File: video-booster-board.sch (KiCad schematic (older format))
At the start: 133 parts, among them IC1 INA180A1IDBVT, J1 0473460001, J10 M20-9990246, J11 MC-HVT1-S04-G, J2 HDMI-PE10-19-LF, J3 HDMI-PE10-19-LF, J6 685119134923_, J9 685119134923_, SW1 1571983-5, U1 PTN3363, U2 TPS2110APW, U3 PTN3363, U4 LP2985-33DBVR, U5 NTS0102GT, U6 EFM32HG321, U7 NTS0102GT

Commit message: Added pulldown on PWR_CTL_D1 and  TVS protection on USB
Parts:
- removed D10: RCLAMP0524PATCT, video-booster-board-footprints:UFDFN-10_2.5x1mm, symbol video-booster-board:RCLAMP0524PATCT
- added D10, D11: RCLAMP0524PATCT_, video-booster-board-footprints:UFDFN-10_2.5x1mm, symbol video-booster-board:RCLAMP0524PATCT_
- added R60: R_100k_0402, video-booster-board-footprints:0402-res, symbol video-booster-board:R_100k_0402-
- C1, C36: symbol video-booster-board:C_4u7_0603-antmicroCapacitors0603 -> video-booster-board:C_4u7_0603-
- C10, C11, C12, C13, C14, C15, C16, C18, C19, C2, C20, C21, C22, C23, C24, C25, C27, C3, C31, C32, C33, C35, C38, C39, C40, C7, C8, C9: symbol video-booster-board:C_100n_0402_6V3-antmicroCapacitors0402 -> video-booster-board:C_100n_0402_6V3-
- C17, C4: symbol video-booster-board:C_10u_0603-antmicroCapacitors0603 -> video-booster-board:C_10u_0603-
- C26, C34, C37, C5, C6: symbol video-booster-board:C_1u_0402-antmicroCapacitors0402 -> video-booster-board:C_1u_0402-
- C28, C30: symbol video-booster-board:C_2u2_0402-antmicroCapacitors0402 -> video-booster-board:C_2u2_0402-
- C29: symbol video-booster-board:C_10n_0402-antmicroCapacitors0402 -> video-booster-board:C_10n_0402-
- J1: symbol video-booster-board:0473460001-antmicroUSBDVIHDMIConnectors -> video-booster-board:0473460001-
- J11: symbol video-booster-board:MC-HVT1-S04-G-antmicroRectangularConnectorsHeadersMalePins -> video-booster-board:MC-HVT1-S04-G-
- J2, J3: symbol video-booster-board:HDMI-PE10-19-LF-antmicroUSBDVIHDMIConnectors -> video-booster-board:HDMI-PE10-19-LF-
- J6, J9: symbol video-booster-board:685119134923_-antmicroUSBDVIHDMIConnectors -> video-booster-board:685119134923_-
- R1, R2: symbol video-booster-board:R_15R_0402-antmicroResistors0402 -> video-booster-board:R_15R_0402-
- R10, R21, R22, R23, R26, R28, R29, R31, R32, R34, R35, R36, R37, R39, R40, R58, R59, R9: symbol video-booster-board:R_10k_0402-antmicroResistors0402 -> video-booster-board:R_10k_0402-
- R11, R12, R7, R8: symbol video-booster-board:R_0R_0402-antmicroResistors0402 -> video-booster-board:R_0R_0402-
- R13, R17: symbol video-booster-board:R_12k4_0402-antmicroResistors0402 -> video-booster-board:R_12k4_0402-
- R14, R15, R19, R24, R5, R6: symbol video-booster-board:R_100k_0402-antmicroResistors0402 -> video-booster-board:R_100k_0402-
- R3, R33, R42, R43, R44, R45, R46, R47, R48, R49, R50, R51, R52, R53, R54, R55: symbol video-booster-board:R_49R9_0402-antmicroResistors0402 -> video-booster-board:R_49R9_0402-
- U1, U3: symbol video-booster-board:PTN3363-antmicroInterfaceDriversReceiversTransceivers -> video-booster-board:PTN3363-
- U4: symbol video-booster-board:LP2985-33DBVR-antmicroPMICVoltageRegulatorsLinear -> video-booster-board:LP2985-33DBVR-
- U6: symbol video-booster-board:EFM32HG321-antmicroMicrocontrollers -> video-booster-board:EFM32HG321-
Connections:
- net labels added: UDN, UDP
- wire segments 560 -> 574

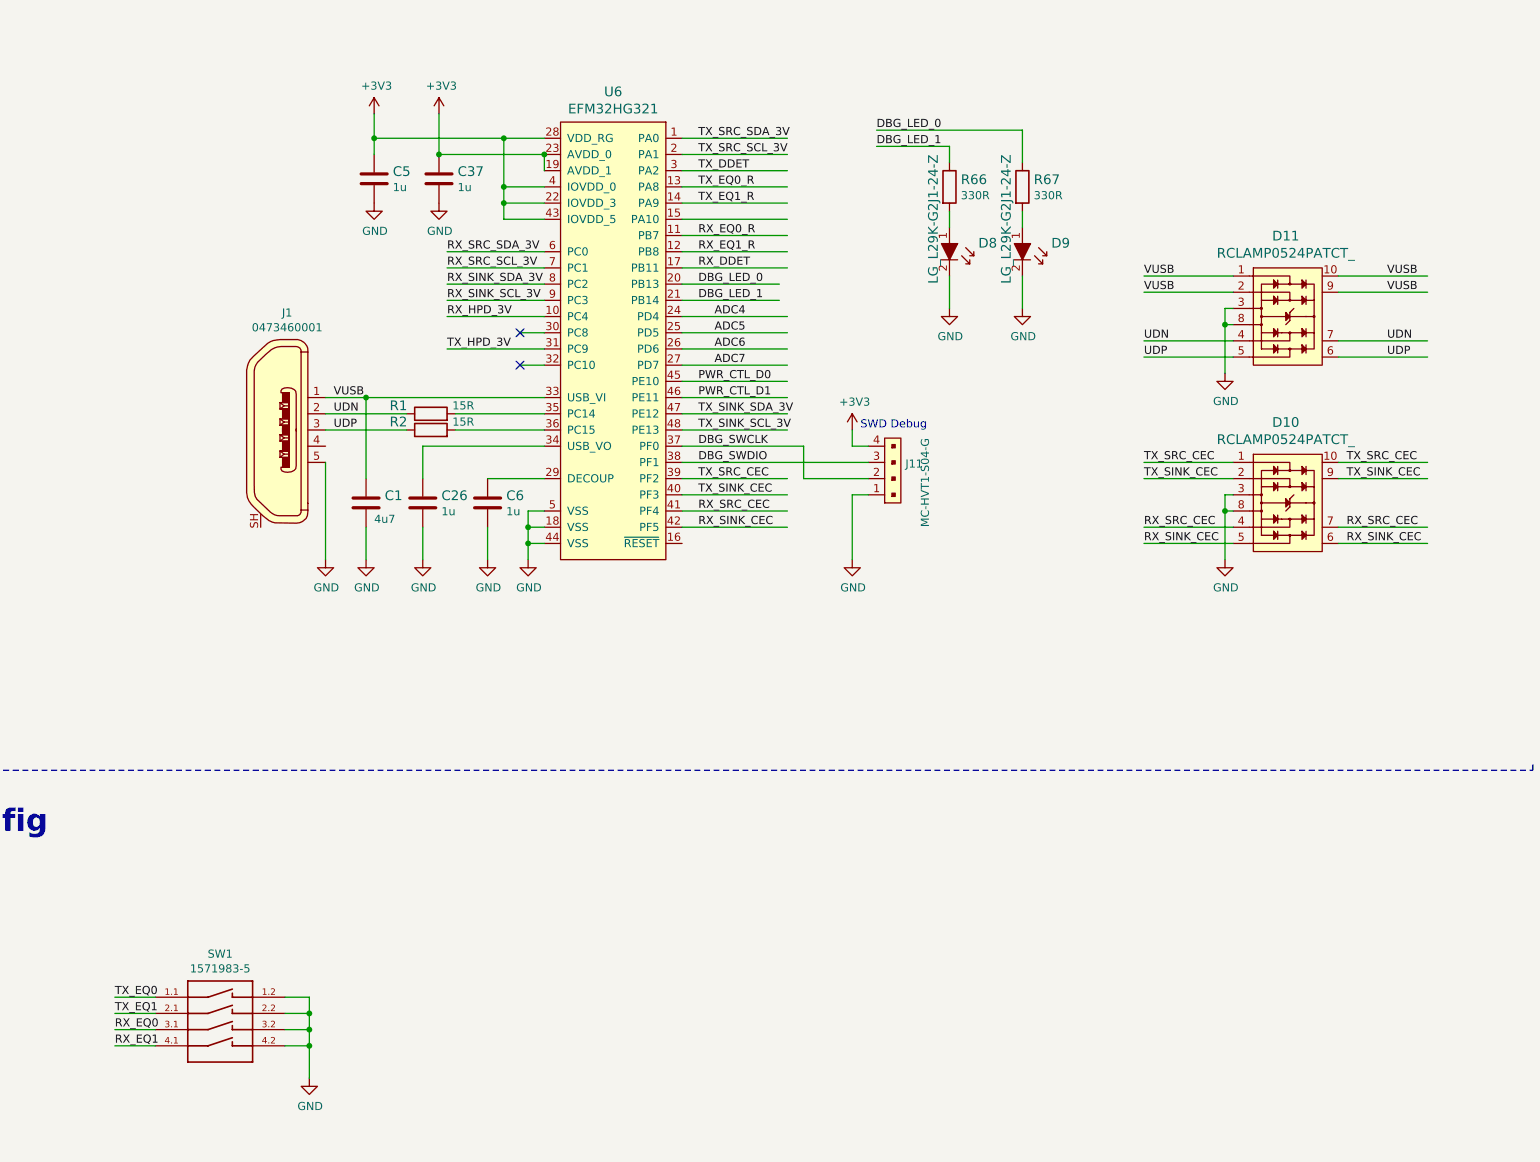
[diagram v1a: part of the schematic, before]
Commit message: PCB routing: HDMI,control, USB
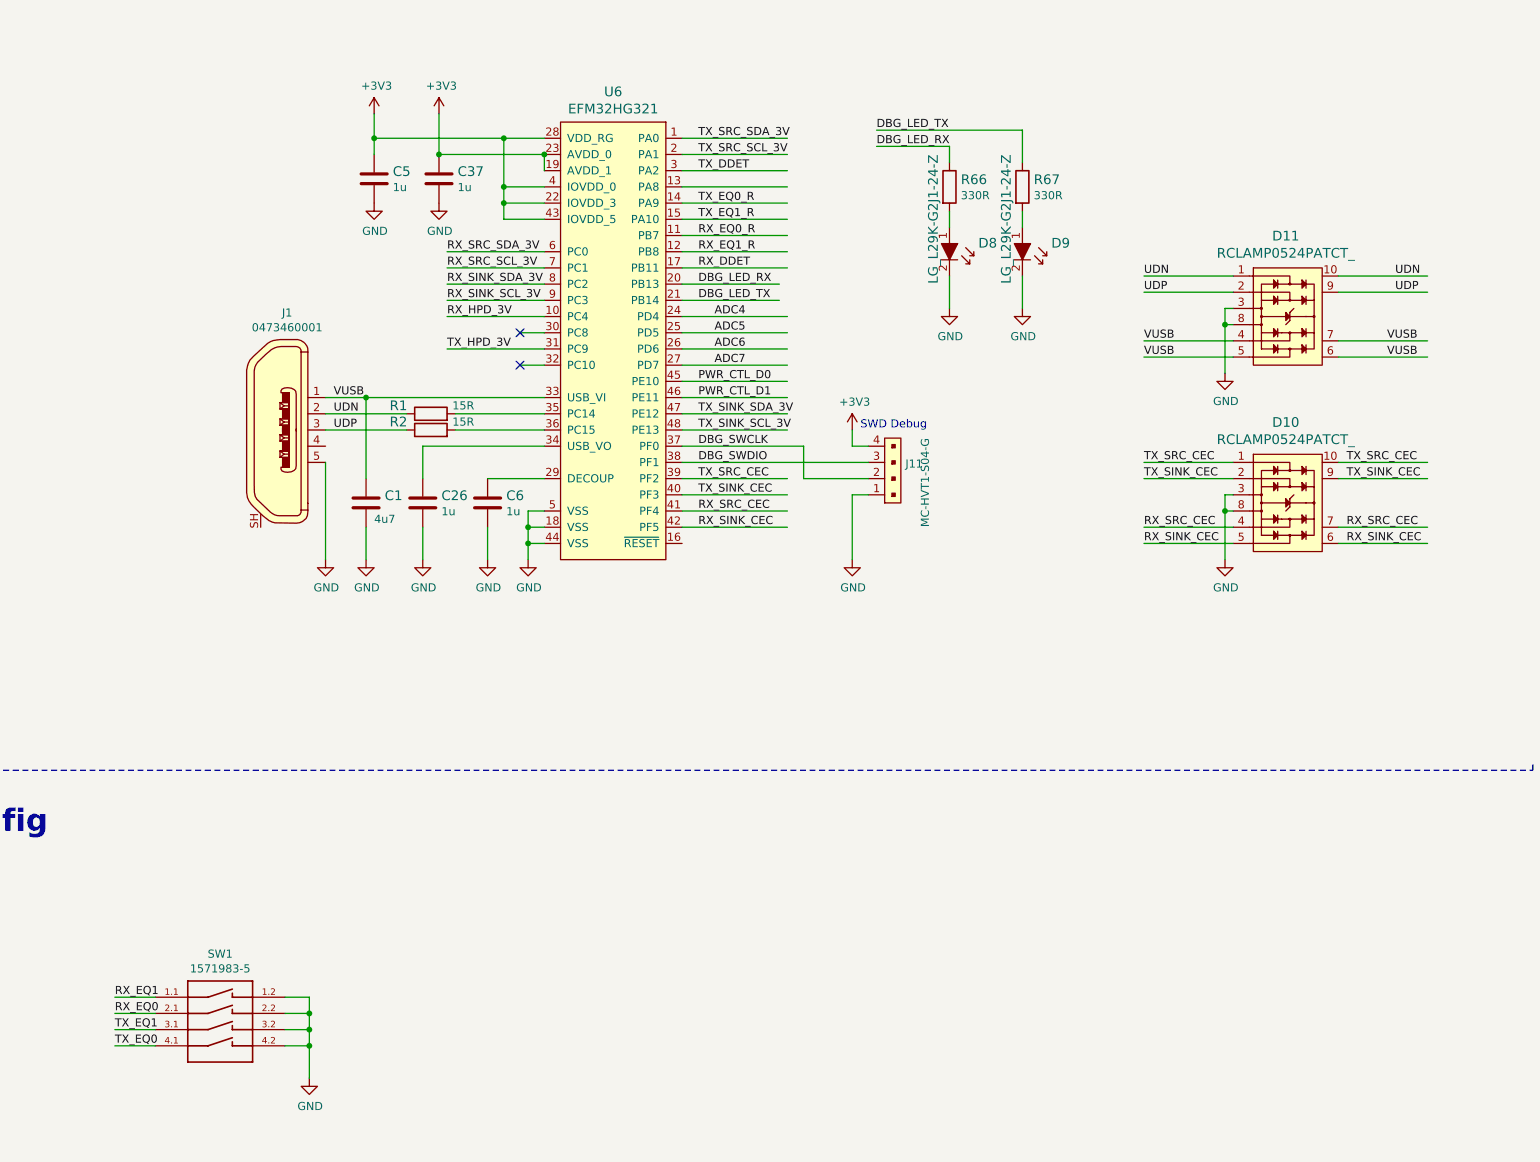
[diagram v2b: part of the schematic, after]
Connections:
- net labels added: DBG_LED_RX, DBG_LED_TX
- net labels removed: DBG_LED_0, DBG_LED_1
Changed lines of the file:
@@
 Wire Wire Line
 	5700 9600 5550 9600
-Text Label 17800 9400 0    50   ~ 0
+Text Label 17800 9500 0    50   ~ 0
 TX_EQ0_R
-Text Label 17800 9500 0    50   ~ 0
+Text Label 17800 9600 0    50   ~ 0
 TX_EQ1_R
 Text Label 17800 9700 0    50   ~ 0
@@
 Wire Wire Line
 	17700 10800 18350 10800
+Text Label 17800 10100 0    50   ~ 0
+DBG_LED_TX
 Text Label 17800 10000 0    50   ~ 0
-DBG_LED_0
-Text Label 17800 10100 0    50   ~ 0
-DBG_LED_1
+DBG_LED_RX
 Wire Wire Line
 	18750 11700 18750 11300
@@
 	16750 11500 16750 11600
 Text Label 18900 9150 0    50   ~ 0
-DBG_LED_1
+DBG_LED_RX
 Text Label 18900 9050 0    50   ~ 0
-DBG_LED_0
+DBG_LED_TX
 Wire Wire Line
 	19800 9050 19800 9250
@@
 Wire Wire Line
 	14200 14700 14450 14700
+Text Label 14200 14700 0    50   ~ 0
+TX_EQ0
+Text Label 14200 14600 0    50   ~ 0
+TX_EQ1
+Text Label 14200 14500 0    50   ~ 0
+RX_EQ0
 Text Label 14200 14400 0    50   ~ 0
-TX_EQ0
-Text Label 14200 14500 0    50   ~ 0
-TX_EQ1
-Text Label 14200 14600 0    50   ~ 0
-RX_EQ0
-Text Label 14200 14700 0    50   ~ 0
 RX_EQ1
 $Comp
@@
 Text Label 15550 10900 0    50   ~ 0
 UDP
+Text Label 20550 10350 0    50   ~ 0
+VUSB
 Text Label 20550 9950 0    50   ~ 0
-VUSB
-Text Label 20550 10350 0    50   ~ 0
 UDN
+Text Label 20550 10050 0    50   ~ 0
+UDP
 Text Label 20550 10450 0    50   ~ 0
-UDP
-Text Label 20550 10050 0    50   ~ 0
-VUSB
-Text Label 22050 9950 0    50   ~ 0
 VUSB
 Text Label 22050 10350 0    50   ~ 0
+VUSB
+Text Label 22100 9950 0    50   ~ 0
 UDN
+Text Label 22100 10050 0    50   ~ 0
+UDP
 Text Label 22050 10450 0    50   ~ 0
-UDP
-Text Label 22050 10050 0    50   ~ 0
 VUSB
 $Comp

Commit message: Routing completed. Minor changes in control pins placement
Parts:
- removed R11, R12, R7, R8: R_0R_0402, video-booster-board-footprints:0402-res, symbol video-booster-board:R_0R_0402-
- removed R22, R28: R_10k_0402, video-booster-board-footprints:0402-res, symbol video-booster-board:R_10k_0402-
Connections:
- wire segments 574 -> 564
- no-connect marks 2 -> 1
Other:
- note removed: "DNP"
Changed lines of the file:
@@
 	0    1    1    0
 $EndComp
-$Comp
-L video-booster-board:R_10k_0402- R22
-U 1 1 5DBDC2E5
-P 4800 5700
-F 0 "R22" V 4650 5750 60  0000 L CNN
-F 1 "R_10k_0402" H 4800 5550 60  0001 C CNN
-F 2 "video-booster-board-footprints:0402-res" H 5000 5900 60  0001 L CNN
-F 3 "" H 4800 5700 50  0001 C CNN
-F 4 "VISHAY" H 5000 6100 60  0001 L CNN "Manufacturer"
-F 5 "CRCW040210K0FKEDHP" H 5000 6000 60  0001 L CNN "MPN"
-F 6 "10k" V 4950 5750 50  0000 L CNN "Val"
-	1    4800 5700
-	0    1    1    0
-$EndComp
 Wire Wire Line
 	4900 6150 4800 6150
@@
 	1    0    0    -1
 $EndComp
-Text Notes 4850 5700 0    50   ~ 10
-DNP
 Text Label 3850 6150 0    50   ~ 0
 TX_HIZ_EN
-Wire Wire Line
-	4800 5850 4800 6150
 Connection ~ 4800 6150
 Wire Wire Line
@@
 Text Label 9800 11400 0    50   ~ 0
 RX_HPD
-$Comp
-L video-booster-board:R_0R_0402- R7
-U 1 1 5E792102
-P 15500 3200
-F 0 "R7" H 15300 3250 60  0000 C CNN
-F 1 "R_0R_0402" H 15500 3050 60  0001 C CNN
-F 2 "video-booster-board-footprints:0402-res" H 15700 3400 60  0001 L CNN
-F 3 "" H 15500 3200 50  0001 C CNN
-F 4 "PANASONIC" H 15700 3600 60  0001 L CNN "Manufacturer"
-F 5 "ERJ2GE0R00X" H 15700 3500 60  0001 L CNN "MPN"
-F 6 "0R" H 15700 3250 50  0000 C CNN "Val"
-	1    15500 3200
-	1    0    0    -1
-$EndComp
-$Comp
-L video-booster-board:R_0R_0402- R8
-U 1 1 5E7927B6
-P 15500 3300
-F 0 "R8" H 15300 3350 60  0000 C CNN
-F 1 "R_0R_0402" H 15500 3150 60  0001 C CNN
-F 2 "video-booster-board-footprints:0402-res" H 15700 3500 60  0001 L CNN
-F 3 "" H 15500 3300 50  0001 C CNN
-F 4 "PANASONIC" H 15700 3700 60  0001 L CNN "Manufacturer"
-F 5 "ERJ2GE0R00X" H 15700 3600 60  0001 L CNN "MPN"
-F 6 "0R" H 15700 3350 50  0000 C CNN "Val"
-	1    15500 3300
-	1    0    0    -1
-$EndComp
-Wire Wire Line
-	16450 3200 15650 3200
-Wire Wire Line
-	15650 3300 16450 3300
 Wire Wire Line
 	3150 3550 2600 3550
 Wire Wire Line
 	3150 3650 2600 3650
-$Comp
-L video-booster-board:R_0R_0402- R11
-U 1 1 5E8A7F00
-P 18200 3200
-F 0 "R11" H 18000 3250 60  0000 C CNN
-F 1 "R_0R_0402" H 18200 3050 60  0001 C CNN
-F 2 "video-booster-board-footprints:0402-res" H 18400 3400 60  0001 L CNN
-F 3 "" H 18200 3200 50  0001 C CNN
-F 4 "PANASONIC" H 18400 3600 60  0001 L CNN "Manufacturer"
-F 5 "ERJ2GE0R00X" H 18400 3500 60  0001 L CNN "MPN"
-F 6 "0R" H 18400 3250 50  0000 C CNN "Val"
-	1    18200 3200
-	1    0    0    -1
-$EndComp
-$Comp
-L video-booster-board:R_0R_0402- R12
-U 1 1 5E8A7F0A
-P 18200 3300
-F 0 "R12" H 18000 3350 60  0000 C CNN
-F 1 "R_0R_0402" H 18200 3150 60  0001 C CNN
-F 2 "video-booster-board-footprints:0402-res" H 18400 3500 60  0001 L CNN
-F 3 "" H 18200 3300 50  0001 C CNN
-F 4 "PANASONIC" H 18400 3700 60  0001 L CNN "Manufacturer"
-F 5 "ERJ2GE0R00X" H 18400 3600 60  0001 L CNN "MPN"
-F 6 "0R" H 18400 3350 50  0000 C CNN "Val"
-	1    18200 3300
-	1    0    0    -1
-$EndComp
 Wire Wire Line
 	3750 13800 4250 13800
@@
 	0    1    1    0
 $EndComp
-$Comp
-L video-booster-board:R_10k_0402- R28
-U 1 1 5ED0E61B
-P 4750 13550
-F 0 "R28" V 4600 13600 60  0000 L CNN
-F 1 "R_10k_0402" H 4750 13400 60  0001 C CNN
-F 2 "video-booster-board-footprints:0402-res" H 4950 13750 60  0001 L CNN
-F 3 "" H 4750 13550 50  0001 C CNN
-F 4 "VISHAY" H 4950 13950 60  0001 L CNN "Manufacturer"
-F 5 "CRCW040210K0FKEDHP" H 4950 13850 60  0001 L CNN "MPN"
-F 6 "10k" V 4900 13600 50  0000 L CNN "Val"
-	1    4750 13550
-	0    1    1    0
-$EndComp
 Wire Wire Line
 	4850 14000 4750 14000
@@
 	1    0    0    -1
 $EndComp
-Text Notes 4800 13550 0    50   ~ 10
-DNP
 Text Label 3800 14000 0    50   ~ 0
 RX_HIZ_EN
-Wire Wire Line
-	4750 13700 4750 14000
 Connection ~ 4750 14000
 Wire Wire Line
@@
 $EndComp
 Wire Wire Line
-	15350 3300 14600 3300
-Wire Wire Line
-	15350 3200 14600 3200
-Wire Wire Line
-	19150 3200 18350 3200
-Wire Wire Line
-	18350 3300 19150 3300
-Wire Wire Line
-	18050 3300 17300 3300
-Wire Wire Line
-	18050 3200 17300 3200
-Text Notes 15450 3150 0    50   ~ 10
-DNP
-Text Notes 15450 3450 0    50   ~ 10
-DNP
-Text Notes 18150 3150 0    50   ~ 10
-DNP
-Text Notes 18150 3450 0    50   ~ 10
-DNP
-Wire Wire Line
 	7400 3850 8050 3850
 Wire Wire Line
@@
 Text Label 16300 4250 0    50   ~ 0
 TX_SRC_SDA
-Text Label 16000 3200 0    50   ~ 0
-TX_SRC_SDA
-Text Label 16000 3300 0    50   ~ 0
-TX_SRC_SCL
-Text Label 14600 3300 0    50   ~ 0
-TX_SINK_SCL
-Text Label 14600 3200 0    50   ~ 0
-TX_SINK_SDA
-Text Label 17300 3200 0    50   ~ 0
-RX_SINK_SDA
-Text Label 17300 3300 0    50   ~ 0
-RX_SINK_SCL
-Text Label 18650 3200 0    50   ~ 0
-RX_SRC_SDA
-Text Label 18650 3300 0    50   ~ 0
-RX_SRC_SCL
 Text Label 5600 14800 0    50   ~ 0
 RX_SRC_SCL
@@
 Text Label 15850 5950 0    50   ~ 0
 TX_SINK_PWR
-Text Label 11100 5750 0    50   ~ 0
-ADC4
 Text Label 8000 5850 0    50   ~ 0
 ADC5
-Text Label 7900 14000 0    50   ~ 0
+Text Label 11100 5750 0    50   ~ 0
 ADC6
 Text Label 17950 6200 0    50   ~ 0
@@
 Wire Wire Line
 	16850 10500 16700 10500
-Wire Wire Line
-	16850 10300 16700 10300
 NoConn ~ 16700 10500
-NoConn ~ 16700 10300
 Wire Wire Line
 	7500 2150 7650 2150
@@
 $EndComp
 $Comp
-L video-booster-board:+3V3 #PWR026
-U 1 1 5DF0F17E
-P 4800 5550
-F 0 "#PWR026" H 4800 5400 50  0001 C CNN
-F 1 "+3V3" H 4815 5723 50  0000 C CNN
-F 2 "" H 4800 5550 50  0001 C CNN
-F 3 "" H 4800 5550 50  0001 C CNN
-	1    4800 5550
-	1    0    0    -1
-$EndComp
-$Comp
 L video-booster-board:+3V3 #PWR032
 U 1 1 5DF0FBA7
@@
 $EndComp
 $Comp
-L video-booster-board:+3V3 #PWR021
-U 1 1 5DFB1DF0
-P 4750 13400
-F 0 "#PWR021" H 4750 13250 50  0001 C CNN
-F 1 "+3V3" H 4765 13573 50  0000 C CNN
-F 2 "" H 4750 13400 50  0001 C CNN
-F 3 "" H 4750 13400 50  0001 C CNN
-	1    4750 13400
-	1    0    0    -1
-$EndComp
-$Comp
 L video-booster-board:+3V3 #PWR030
 U 1 1 5DFB2497
@@
 Wire Wire Line
 	14650 6050 14500 6050
+Text Label 7950 14000 0    50   ~ 0
+ADC4
+Text Label 17800 9400 0    50   ~ 0
+RX_HIZ_EN
+Text Label 16250 10300 0    50   ~ 0
+TX_HIZ_EN
+Wire Wire Line
+	16850 10300 16250 10300
 $EndSCHEMATC
